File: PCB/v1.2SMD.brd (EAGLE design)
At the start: 90 x 80 mm, 48 parts, among them IC1 MEGA8-P

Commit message: Replaced NMos package
replaced CBE with much more common BEC package
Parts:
- T1, T2, T3, T4, T5, T6, T7, T8: device transistor-neu-to92:SOT23-EBC -> transistor:SOT23-BEC
- moved R9 54.4 mm to (21.3, 22.9), turned to 90 degrees
- moved C8 3.30 mm to (77.5, 23.9)
- moved R18 3.30 mm to (74.9, 23.9)
- moved R22 3.30 mm to (80.0, 23.9)
- moved R19 3.05 mm to (70.1, 23.9)
- moved T6 2.81 mm to (25.4, 41.7)
- moved R10 2.79 mm to (77.0, 53.3)
- moved R11 2.79 mm to (74.7, 35.6)
- moved R13 2.79 mm to (77.0, 55.9)
- moved ROTARY_1 2.79 mm to (79.2, 64.8)
- moved ROTARY_2 2.79 mm to (79.2, 44.5)
- moved T5 2.55 mm to (28.7, 44.5)
- moved C1 2.54 mm to (67.6, 49.3)
- moved C2 2.54 mm to (67.6, 46.7)
- moved C3 2.54 mm to (67.6, 59.4)
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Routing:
- net GND: track 163.6 -> 147.4 mm, vias 6 -> 9
- net NFET_KASKODE_4: track 72.3 -> 57.5 mm
- net NFET_KASKODE_2: track 94.4 -> 80.1 mm, vias 1 -> 3
- net NFET_KASKODE_1: track 115.1 -> 101.2 mm
- net VCC: track 561.2 -> 547.6 mm
- net SDA: track 48.7 -> 37.1 mm
- net SCL: track 57.9 -> 47.1 mm
- net NFET_KASKODE_3: track 62.4 -> 67.0 mm
- net RE1_1: track 44.6 -> 40.4 mm
- net RE1_2: track 37.7 -> 34.0 mm
- net RESET: track 90.8 -> 87.5 mm
- net RE2_2: track 39.2 -> 36.4 mm
- net RE2_1: track 42.4 -> 40.0 mm
- net N$5: track 7.77 -> 9.17 mm
- net N$9: track 4.04 -> 2.70 mm
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
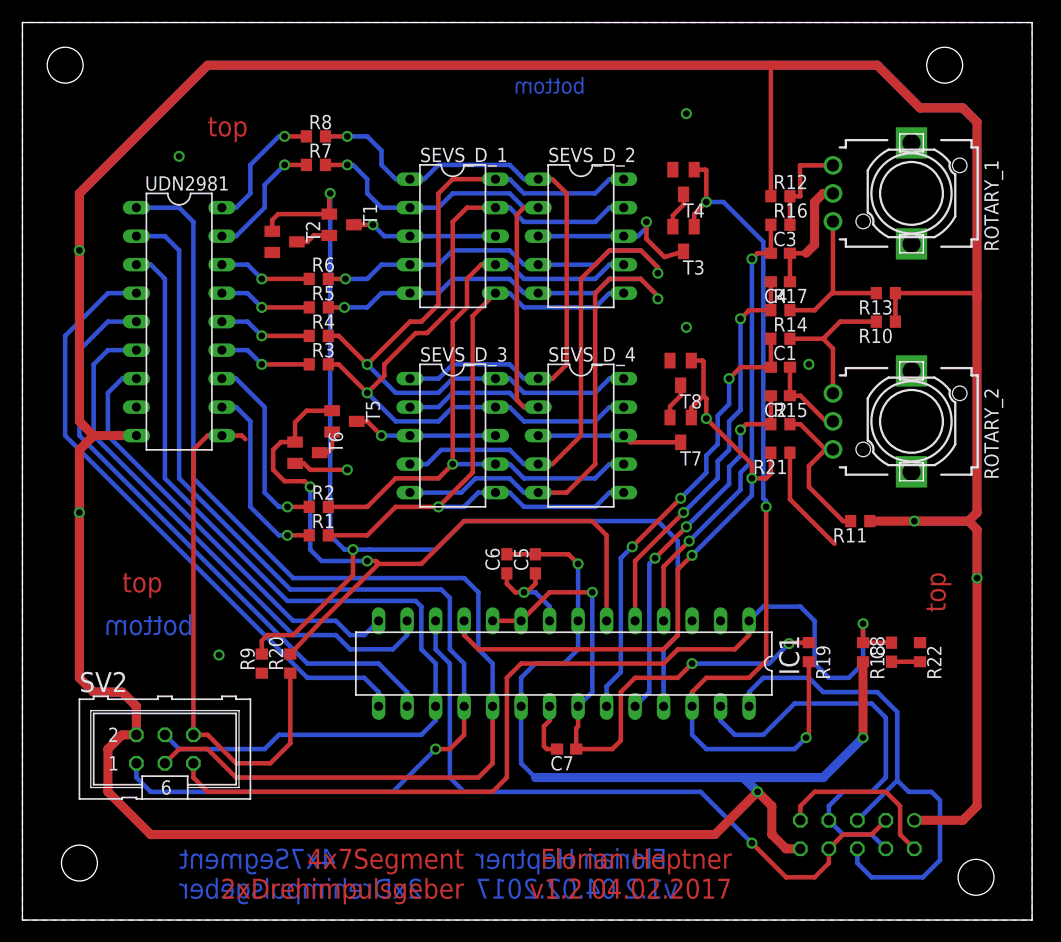
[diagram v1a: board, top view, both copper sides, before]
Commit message: routing
optimized some routes
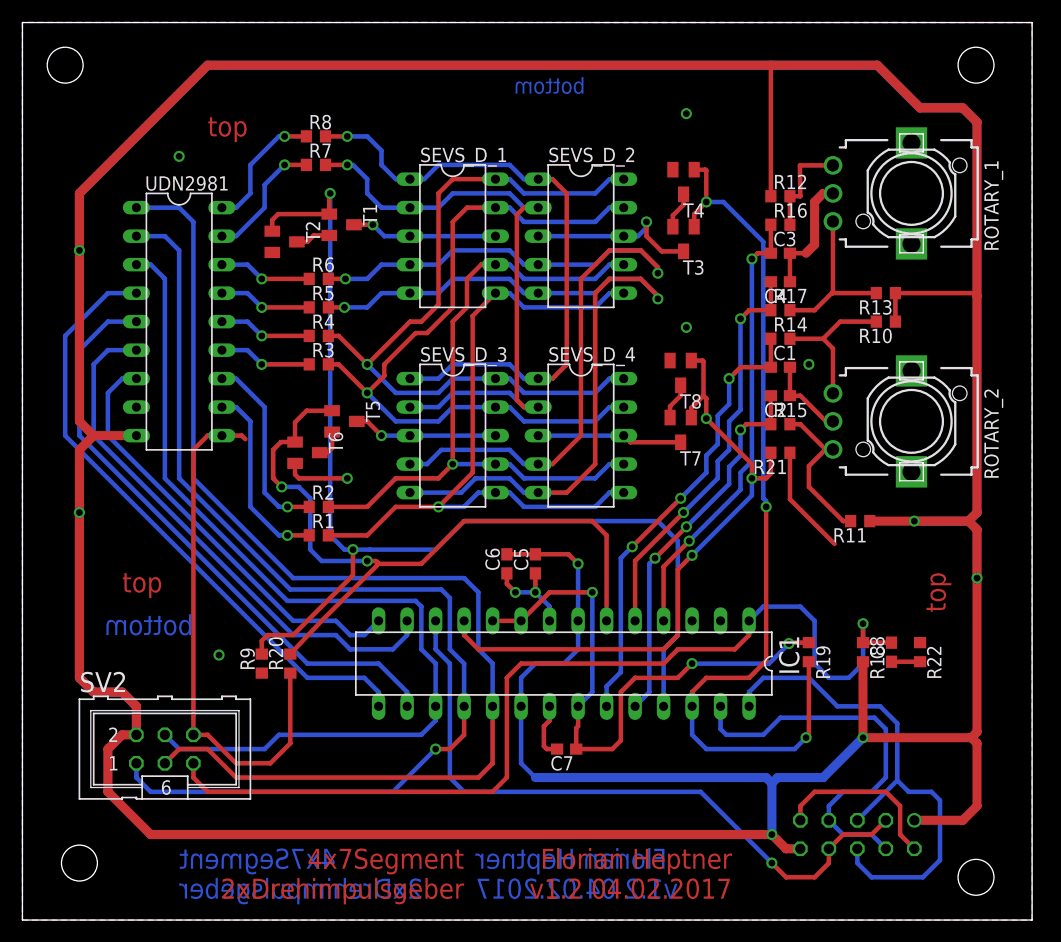
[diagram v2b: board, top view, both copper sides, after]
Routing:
- net VCC: track 547.6 -> 556.2 mm
- net SDA: track 37.1 -> 35.9 mm
- net GND: track 147.4 -> 148.3 mm
- net SCL: track 47.1 -> 46.5 mm
- net N$12: track 9.11 -> 8.54 mm, vias 1 -> 2

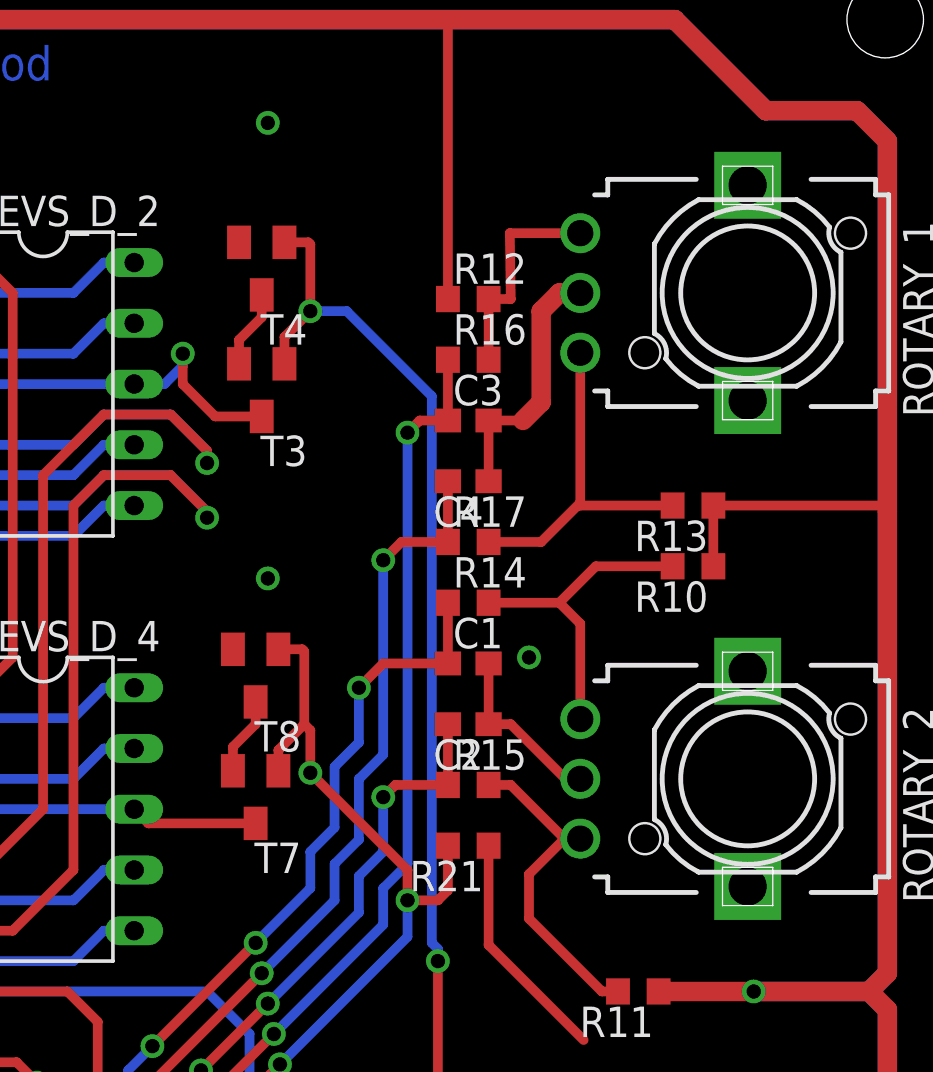
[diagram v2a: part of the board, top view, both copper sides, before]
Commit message: diameter correction
corrected diameter for rotary encoder
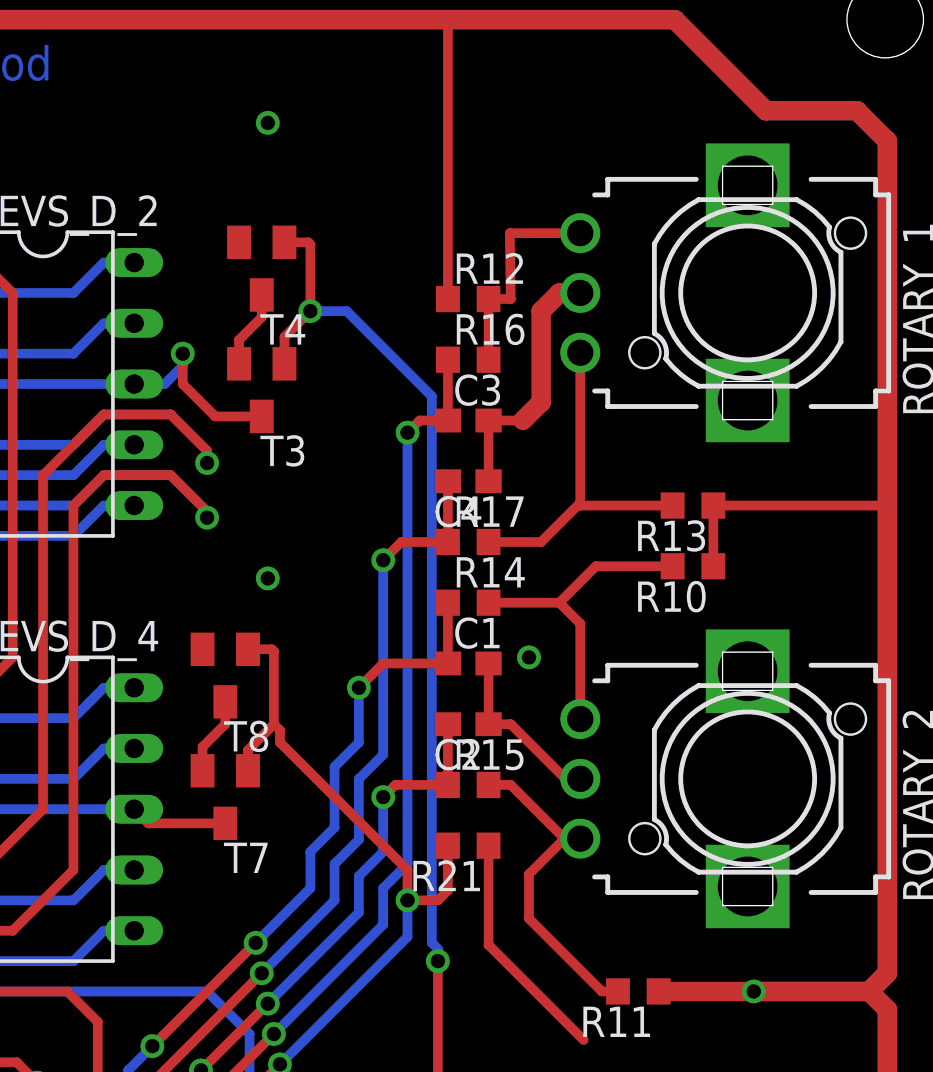
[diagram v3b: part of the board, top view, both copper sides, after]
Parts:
- moved T7 1.27 mm to (57.4, 43.7)
- moved T8 1.27 mm to (57.4, 48.8)
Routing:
- net S_EN_4: track 12.9 -> 11.7 mm
- net NFET_KASKODE_4: track 57.5 -> 58.0 mm, vias 3 -> 2
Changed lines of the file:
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@@
 <element name="T5" library="transistor" package="SOT23-BEC" value="" x="28.702" y="44.45" rot="R270"/>
 <element name="T6" library="transistor" package="SOT23-BEC" value="" x="25.4" y="41.656" rot="R270"/>
-<element name="T7" library="transistor" package="SOT23-BEC" value="" x="58.674" y="43.688" rot="R180"/>
-<element name="T8" library="transistor" package="SOT23-BEC" value="" x="58.674" y="48.768" rot="R180"/>
+<element name="T7" library="transistor" package="SOT23-BEC" value="" x="57.404" y="43.688" rot="R180"/>
+<element name="T8" library="transistor" package="SOT23-BEC" value="" x="57.404" y="48.768" rot="R180"/>
 <element name="R22" library="rcl" package="R0603" value="1k" x="80.01" y="23.876" rot="R270"/>
 <element name="SV1" library="con-lsta" package="FE05-2" value="" x="74.422" y="7.62" rot="MR0">
@@
 <wire x1="66.714" y1="39.79" x2="66.294" y2="39.37" width="0.4064" layer="1"/>
 <via x="65.024" y="39.37" extent="1-16" drill="0.6" shape="octagon"/>
-<wire x1="59.624" y1="44.788" x2="59.624" y2="45.654" width="0.4064" layer="1"/>
-<wire x1="59.624" y1="45.654" x2="60.706" y2="46.736" width="0.4064" layer="1"/>
-<wire x1="60.706" y1="46.736" x2="60.706" y2="49.784" width="0.4064" layer="1"/>
-<wire x1="60.706" y1="49.784" x2="60.622" y2="49.868" width="0.4064" layer="1"/>
-<wire x1="60.622" y1="49.868" x2="59.624" y2="49.868" width="0.4064" layer="1"/>
-<via x="60.96" y="44.704" extent="1-16" drill="0.6" shape="octagon"/>
-<wire x1="60.96" y1="44.704" x2="60.96" y2="46.482" width="0.4064" layer="1"/>
-<wire x1="60.96" y1="46.482" x2="60.706" y2="46.736" width="0.4064" layer="1"/>
+<wire x1="58.354" y1="44.788" x2="58.354" y2="45.654" width="0.4064" layer="1"/>
+<wire x1="58.354" y1="45.654" x2="59.436" y2="46.736" width="0.4064" layer="1"/>
+<wire x1="59.436" y1="46.736" x2="59.436" y2="49.784" width="0.4064" layer="1"/>
+<wire x1="59.436" y1="49.784" x2="59.352" y2="49.868" width="0.4064" layer="1"/>
+<wire x1="59.352" y1="49.868" x2="58.354" y2="49.868" width="0.4064" layer="1"/>
+<wire x1="59.69" y1="46.482" x2="59.436" y2="46.736" width="0.4064" layer="1"/>
 <wire x1="58.42" y1="31.242" x2="59.69" y2="32.512" width="0.4064" layer="1"/>
 <via x="59.69" y="32.512" extent="1-16" drill="0.6" shape="octagon"/>
 <wire x1="59.69" y1="32.512" x2="65.024" y2="37.846" width="0.4064" layer="16"/>
 <wire x1="65.024" y1="37.846" x2="65.024" y2="39.37" width="0.4064" layer="16"/>
-<wire x1="60.96" y1="44.704" x2="65.024" y2="40.64" width="0.4064" layer="1"/>
 <wire x1="65.024" y1="40.64" x2="65.024" y2="39.37" width="0.4064" layer="1"/>
 <wire x1="65.024" y1="39.37" x2="66.294" y2="39.37" width="0.4064" layer="1"/>
+<wire x1="59.69" y1="46.482" x2="59.69" y2="45.974" width="0.4064" layer="1"/>
+<wire x1="59.69" y1="45.974" x2="65.024" y2="40.64" width="0.4064" layer="1"/>
 </signal>
 <signal name="S_EN_4">
@@
 <wire x1="45.974" y1="43.18" x2="53.594" y2="43.18" width="0.4064" layer="16"/>
 <contactref element="T7" pad="C"/>
-<wire x1="58.674" y1="42.588" x2="54.186" y2="42.588" width="0.4064" layer="1"/>
+<wire x1="57.404" y1="42.588" x2="54.186" y2="42.588" width="0.4064" layer="1"/>
 <wire x1="54.186" y1="42.588" x2="53.594" y2="43.18" width="0.4064" layer="1"/>
 </signal>
@@
 <contactref element="T7" pad="E"/>
 <contactref element="T8" pad="C"/>
-<wire x1="58.674" y1="47.668" x2="58.674" y2="46.736" width="0.4064" layer="1"/>
-<wire x1="58.674" y1="46.736" x2="57.724" y2="45.786" width="0.4064" layer="1"/>
-<wire x1="57.724" y1="45.786" x2="57.724" y2="44.788" width="0.4064" layer="1"/>
+<wire x1="57.404" y1="47.668" x2="57.404" y2="46.736" width="0.4064" layer="1"/>
+<wire x1="57.404" y1="46.736" x2="56.454" y2="45.786" width="0.4064" layer="1"/>
+<wire x1="56.454" y1="45.786" x2="56.454" y2="44.788" width="0.4064" layer="1"/>
 </signal>
 <signal name="N$2">
